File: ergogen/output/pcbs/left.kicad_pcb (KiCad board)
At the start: 2 copper layers, 144.4 x 121 mm, 69 parts

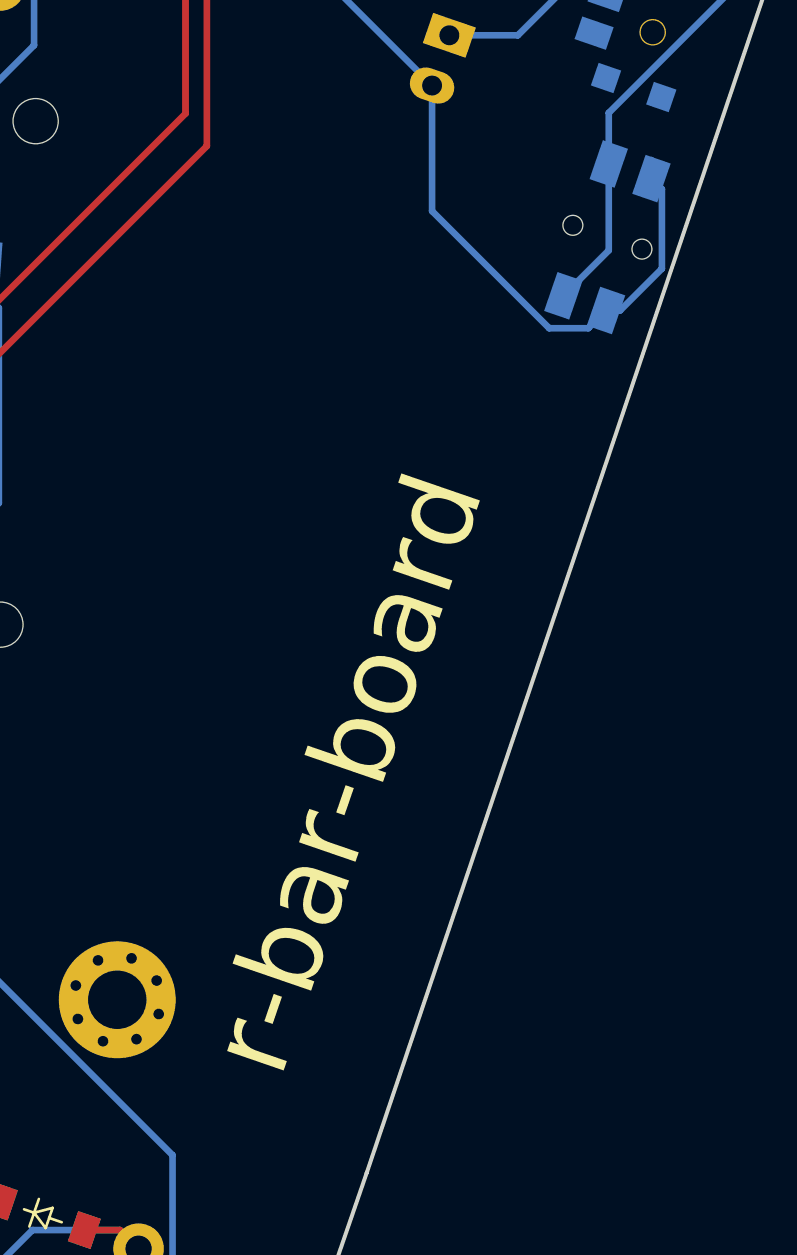
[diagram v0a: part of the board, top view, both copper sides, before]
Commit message: rename with underscores
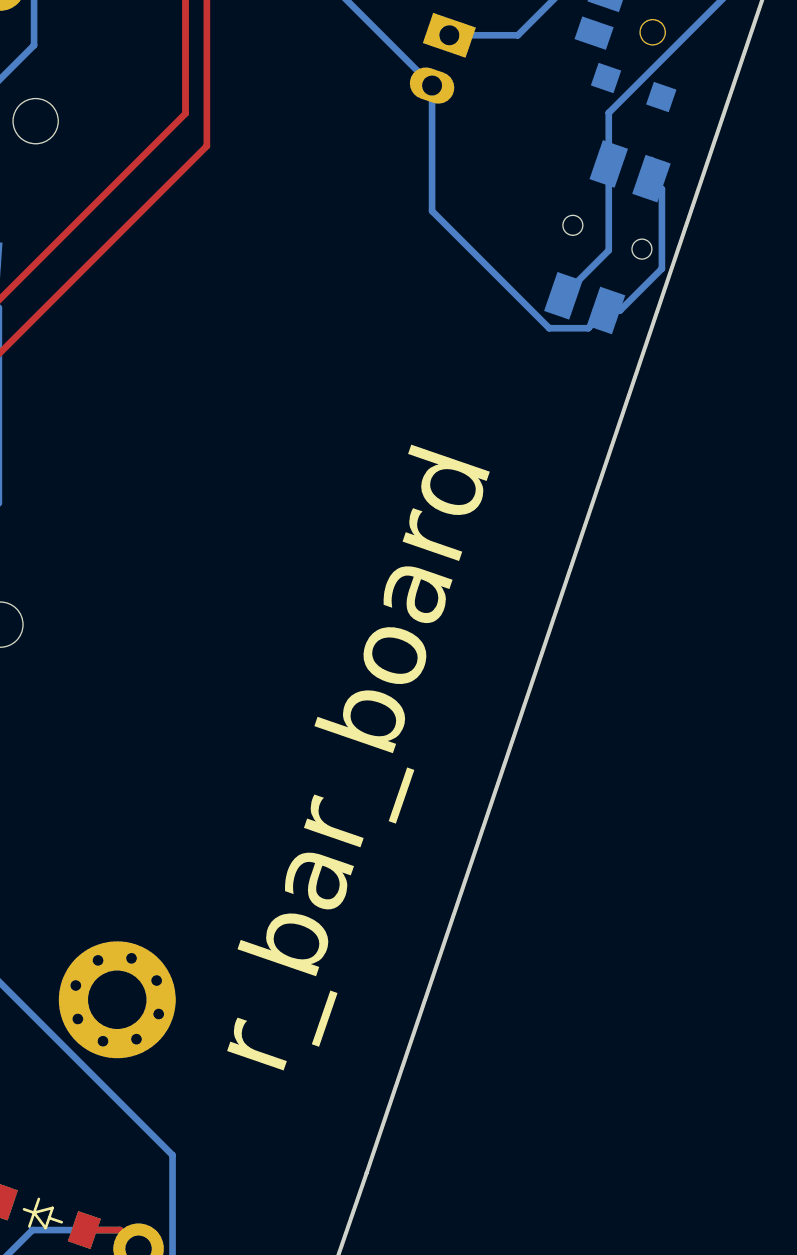
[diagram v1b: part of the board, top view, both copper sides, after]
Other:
- board text added: "r_bar_board"
- board text removed: "r-bar-board"
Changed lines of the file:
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@@
 		(layer "Edge.Cuts")
 	)
-	(gr_text "r-bar-board"
+	(gr_text "r_bar_board"
 		(at 160.655815 200.420244 71)
 		(layer "F.SilkS")
